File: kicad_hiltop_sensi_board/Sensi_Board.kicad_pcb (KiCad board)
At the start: 4 copper layers, 159.9 x 99.9 mm, 354 parts, among them J1 Conn_02x06_Counter_Clockwise, J10 Conn_ARM_JTAG_SWD_10, J2 Conn_02x06_Counter_Clockwise, J3 Conn_03x32_DIN41612, J4 Conn_02x06_Counter_Clockwise, J5 Conn_02x06_Counter_Clockwise, J6 Conn_02x06_Counter_Clockwise, J7 Conn_02x06_Counter_Clockwise, J8 Conn_02x06_Counter_Clockwise, K1 HRS1KH-S, Q10 ZXMN6A07F, Q11 ZXMN6A07F, Q2 ZXMN6A07F, Q7 ZXMN6A07F, Q8 ZXMN6A07F, SW1 SW_Push, SW2 SW_DIP_x04, SW3 SW_DIP_x04, SW4 SW_DIP_x04, SW5 SW_DIP_x04, U1 INA250A4, U10 MAX31865, U11 MAX31865, U13 CP2102N-A01-GQFN24, U14 BTS4140N, U15 BTS4140N, U16 MAX4194, U17 BTS4140N, U18 BTS4140N, U19 MAX4194, U2 LD1117S33TR_SOT223, U20 MAX4194, U21 MAX4194, U22 STM32F072RBTx, U23 MAX4194, U24 MAX4194, U25 MAX4194, U26 MAX4194, U27 USB2502, U3 AT25DN512CSSHF-B, U4 AD8646, U5 AD8646, U6 LM75B, U7 AT24C02C-SSHM-T, U8 MAX31865, U9 MAX31865, Y1 50ppm 24.000MHZ, Y2 8MHZ, Y3 ABS25-32.768KHZ-6-T

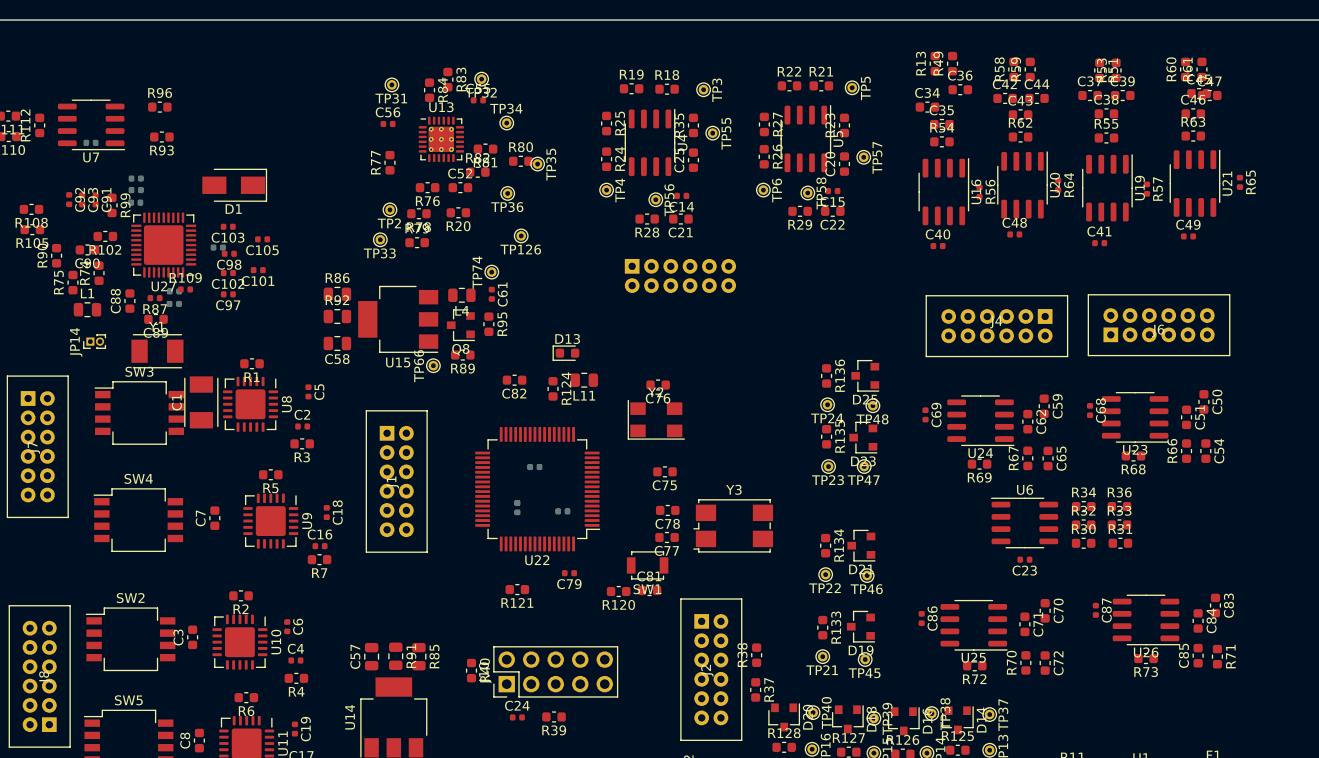
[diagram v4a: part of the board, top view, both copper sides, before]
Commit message: Updated sensi board pin map and layout before PCB tracking
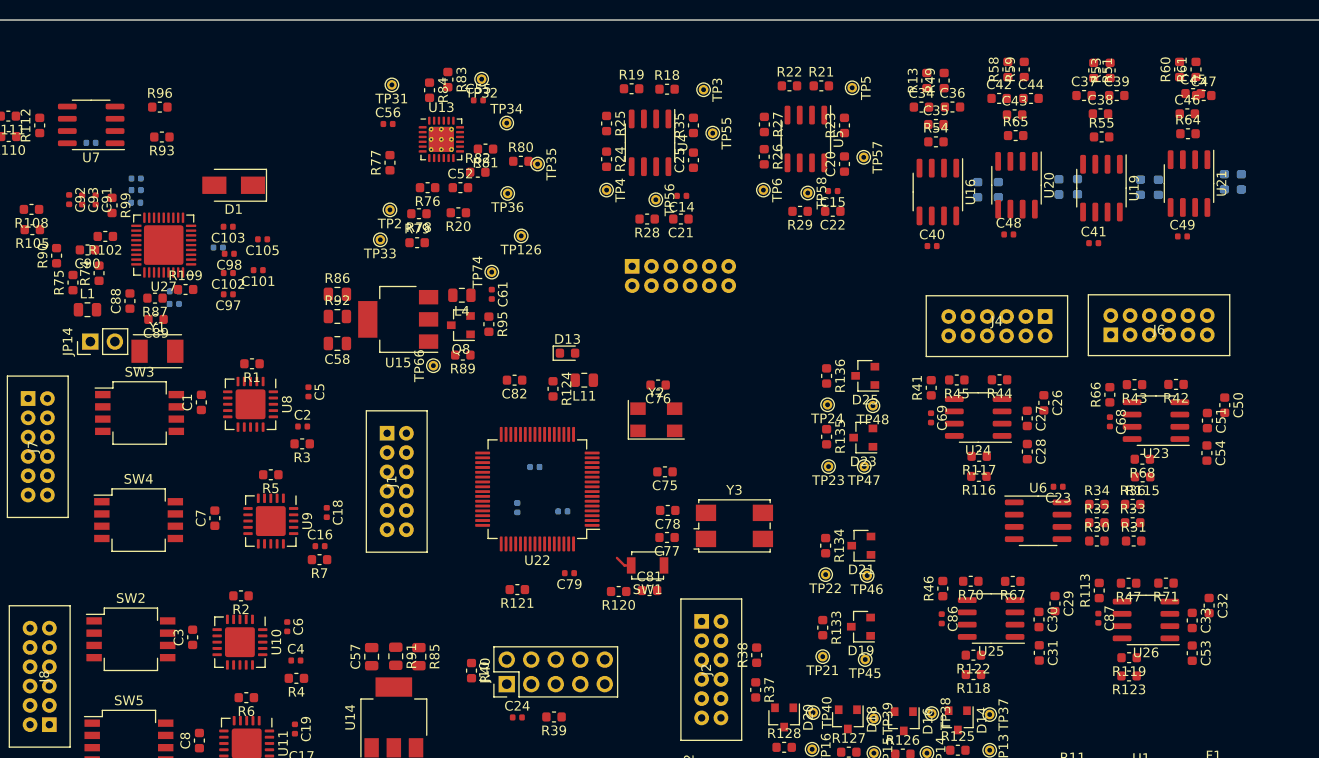
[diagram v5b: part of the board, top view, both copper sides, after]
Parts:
- removed C59, C65, C70, C72, C83, C85: Ccm, Capacitor_SMD:C_0603_1608Metric
- removed C62, C71, C84: Cdiff, Capacitor_SMD:C_0603_1608Metric
- added C26: Ccm, Capacitor_SMD:C_0603_1608Metric, F.Cu at (177.7, 84.8)
- added C27: Cdiff, Capacitor_SMD:C_0603_1608Metric, F.Cu at (175.9, 86.4)
- added C28: Ccm, Capacitor_SMD:C_0603_1608Metric, F.Cu at (175.9, 89.8)
- added C29: Ccm, Capacitor_SMD:C_0603_1608Metric, F.Cu at (178.8, 105.5)
- added C30: Cdiff, Capacitor_SMD:C_0603_1608Metric, F.Cu at (177.2, 107.2)
- added C31: Ccm, Capacitor_SMD:C_0603_1608Metric, F.Cu at (177.2, 110.7)
- added C32: Ccm, Capacitor_SMD:C_0603_1608Metric, F.Cu at (194.8, 105.8)
- added C33: Cdiff, Capacitor_SMD:C_0603_1608Metric, F.Cu at (193.0, 107.3)
- added C53: Ccm, Capacitor_SMD:C_0603_1608Metric, F.Cu at (193.0, 110.7)
- added R113: R, Resistor_SMD:R_0603_1608Metric, F.Cu at (183.4, 104.2)
- added R114: DNF, Resistor_SMD:R_0603_1608Metric, B.Cu at (181.2, 62.4)
- added R115: DNF, Resistor_SMD:R_0603_1608Metric, F.Cu at (187.9, 92.4)
- added R116: DNF, Resistor_SMD:R_0603_1608Metric, F.Cu at (170.9, 92.4)
- added R117: R, Resistor_SMD:R_0603_1608Metric, F.Cu at (171.0, 90.3)
- added R118: DNF, Resistor_SMD:R_0603_1608Metric, F.Cu at (170.4, 112.9)
- added R119: DNF, Resistor_SMD:R_0603_1608Metric, F.Cu at (186.5, 111.2)
- added R122: R, Resistor_SMD:R_0603_1608Metric, F.Cu at (170.4, 110.9)
- added R123: R, Resistor_SMD:R_0603_1608Metric, F.Cu at (186.5, 113.0)
- added R41: 0R, Resistor_SMD:R_0603_1608Metric, F.Cu at (166.0, 83.2)
- added R42: R, Resistor_SMD:R_0603_1608Metric, F.Cu at (191.4, 82.8)
- added R43: R, Resistor_SMD:R_0603_1608Metric, F.Cu at (187.1, 82.9)
- added R44: R, Resistor_SMD:R_0603_1608Metric, F.Cu at (173.1, 82.4)
- added R45: R, Resistor_SMD:R_0603_1608Metric, F.Cu at (168.6, 82.4)
- added R46: 0R, Resistor_SMD:R_0603_1608Metric, F.Cu at (167.2, 104.0)
- added R47: 0R, Resistor_SMD:R_0603_1608Metric, F.Cu at (186.4, 103.4)
- C1: footprint Crystal:Crystal_SMD_TXC_7A-2Pin_5x3.2mm -> Capacitor_SMD:C_0603_1608Metric
- C100, C102, C103, C104, C105: value 4.7uF 6.3V X5R -> 4.7uF
- C57, C58, C63, C64, R85, R86, R97, R98: value DNP -> DNF
- C91: value 1.0uF X5R 16V -> 1.0uF
- JP14: footprint Connector_PinHeader_1.00mm:PinHeader_1x02_P1.00mm_Vertical -> Connector_PinHeader_2.54mm:PinHeader_1x02_P2.54mm_Vertical
- L1: value FB 500mA/0.10DCR -> 500mA/0.10DCR
- R109, R87: footprint Resistor_SMD:R_0402_1005Metric -> Resistor_SMD:R_0603_1608Metric
- R56, R57: value 12K5 -> 12.4K; footprint Resistor_SMD:R_0402_1005Metric -> Resistor_SMD:R_0603_1608Metric; moved to B.Cu
- R62, R63: value 32R -> DNF; moved to B.Cu
- R64, R65: value 12K5 -> 32R; footprint Resistor_SMD:R_0402_1005Metric -> Resistor_SMD:R_0603_1608Metric
- R67, R70, R71: value 0R -> R
- R69: value 100R 0.1% -> 12.4K; moved to B.Cu
- R72: value R -> 12.4K; moved to B.Cu
- R73: value R -> DNF; moved to B.Cu
- moved R72 50.4 mm to (179.2, 62.4), turned to 270 degrees
- moved R73 50.4 mm to (198.1, 61.9), turned to 270 degrees
- moved R69 38.7 mm to (196.4, 61.8), turned to 270 degrees
- moved R65 23.7 mm to (174.7, 57.0), turned to 0 degrees
- moved R64 14.5 mm to (192.6, 56.9), turned to 0 degrees
- moved R67 12.8 mm to (174.4, 103.2), turned to 180 degrees
- moved R70 10.2 mm to (170.1, 103.2), turned to 180 degrees
- moved R66 9.86 mm to (184.5, 83.9)
- moved R71 9.30 mm to (190.3, 103.4), turned to 180 degrees
- moved C23 8.31 mm to (179.1, 93.4)
- moved R63 6.43 mm to (189.5, 62.4), turned to 270 degrees
- moved R62 5.93 mm to (172.9, 62.7), turned to 270 degrees
- moved C68 2.37 mm to (184.5, 86.7)
- moved C51 2.19 mm to (194.6, 86.6)
- moved U23 2.19 mm to (189.3, 86.6)
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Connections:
- net /STM_Micro/ADC13 renamed /STM_Micro/ADC8
- C20 pad 2: /ADC11 -> /ADC12
- C21 pad 2: /ADC10 -> /ADC13
- C22 pad 2: /ADC12 -> /ADC6
- C25 pad 2: /ADC9 -> /ADC7
- C50 pad 2: /TH1+ -> Net-(C50-Pad2)
- C51 pad 1: /TH1+ -> Net-(C50-Pad2)
- C51 pad 2: /TH1- -> Net-(C51-Pad2)
- C54 pad 1: /TH1- -> Net-(C51-Pad2)
- J5 pad 1: /ADC9 -> /ADC7
- J5 pad 12: /ADC12 -> /ADC6
- J5 pad 3: /ADC10 -> /ADC13
- J5 pad 5: /ADC11 -> /ADC12
- R23 pad 1: /ADC11 -> /ADC12
- R28 pad 1: /ADC10 -> /ADC13
- R29 pad 1: /ADC12 -> /ADC6
- R35 pad 1: /ADC9 -> /ADC7
- R62 pad 1: Net-(C42-Pad2) -> Net-(R56-Pad1)
- R62 pad 2: Net-(C43-Pad2) -> Net-(R56-Pad2)
- R63 pad 1: Net-(C45-Pad2) -> Net-(R57-Pad1)
- R63 pad 2: Net-(C46-Pad2) -> Net-(R57-Pad2)
- R64 pad 1: Net-(R64-Pad1) -> Net-(C45-Pad2)
- R64 pad 2: Net-(R64-Pad2) -> Net-(C46-Pad2)
- R65 pad 1: Net-(R65-Pad1) -> Net-(C42-Pad2)
- R65 pad 2: Net-(R65-Pad2) -> Net-(C43-Pad2)
- R67 pad 1: GND -> Net-(C29-Pad2)
- R67 pad 2: /TH3- -> /TH4+
- R70 pad 1: GND -> Net-(C30-Pad2)
- R71 pad 1: GND -> Net-(C32-Pad2)
- R71 pad 2: /TH2- -> /TH2+
- R72 pad 1: Net-(R72-Pad1) -> Net-(R114-Pad1)
- R72 pad 2: Net-(R72-Pad2) -> Net-(R114-Pad2)
- R73 pad 1: Net-(R73-Pad1) -> Net-(R69-Pad1)
- R73 pad 2: Net-(R73-Pad2) -> Net-(R69-Pad2)
- TP55 pad 1: /ADC9 -> /ADC7
- TP56 pad 1: /ADC10 -> /ADC13
- TP57 pad 1: /ADC11 -> /ADC12
- TP58 pad 1: /ADC12 -> /ADC6
- U16 pad 6: /ADC8 -> /ADC5
- U19 pad 6: /ADC6 -> /ADC3
- U20 pad 1: Net-(R64-Pad1) -> Net-(R114-Pad1)
- U20 pad 6: /ADC7 -> /ADC4
- U20 pad 8: Net-(R64-Pad2) -> Net-(R114-Pad2)
- U21 pad 1: Net-(R65-Pad1) -> Net-(R69-Pad1)
- U21 pad 6: /ADC5 -> /ADC2
- U21 pad 8: Net-(R65-Pad2) -> Net-(R69-Pad2)
- U22 pad 10: /ADC3 -> /ADC10
- U22 pad 11: /ADC2 -> /ADC11
- U22 pad 16: /ADC5 -> /ADC2
- U22 pad 17: /ADC6 -> /ADC3
- U22 pad 20: /ADC7 -> /ADC4
- U22 pad 22: /ADC8 -> /ADC5
- U22 pad 23: /ADC12 -> /ADC6
- U22 pad 24: /ADC11 -> /ADC12
- U22 pad 25: /ADC10 -> /ADC13
- U22 pad 26: /STM_RES2 -> /STM_RES1
- U22 pad 27: /ADC9 -> /ADC7
- U22 pad 28: /GPIO3 -> /STM_RES2
- U22 pad 40: /STM_RES1 -> /GPIO3
- U22 pad 51: Net-(R121-Pad2) -> (no net)
- U22 pad 53: (no net) -> Net-(R121-Pad2)
- U22 pad 9: /ADC4 -> /ADC9
- U23 pad 2: /TH1- -> Net-(C51-Pad2)
- U23 pad 3: /TH1+ -> Net-(C50-Pad2)
- U23 pad 6: /ADC2 -> /ADC11
- U24 pad 1: Net-(R69-Pad1) -> Net-(R116-Pad1)
- U24 pad 2: /TH3- -> Net-(C27-Pad2)
- U24 pad 3: /TH3+ -> Net-(C26-Pad2)
- U24 pad 8: Net-(R69-Pad2) -> Net-(R116-Pad2)
- U25 pad 1: Net-(R72-Pad1) -> Net-(R118-Pad1)
- U25 pad 2: /TH4- -> Net-(C30-Pad2)
- U25 pad 3: /TH4+ -> Net-(C29-Pad2)
- U25 pad 6: /ADC4 -> /ADC9
- U25 pad 8: Net-(R72-Pad2) -> Net-(R118-Pad2)
- U26 pad 1: Net-(R73-Pad1) -> Net-(R119-Pad1)
- U26 pad 2: /TH2- -> Net-(C33-Pad2)
- U26 pad 3: /TH2+ -> Net-(C32-Pad2)
- U26 pad 6: /ADC3 -> /ADC10
- U26 pad 8: Net-(R73-Pad2) -> Net-(R119-Pad2)
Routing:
- net /STM_RESET: track 0.00 -> 1.80 mm

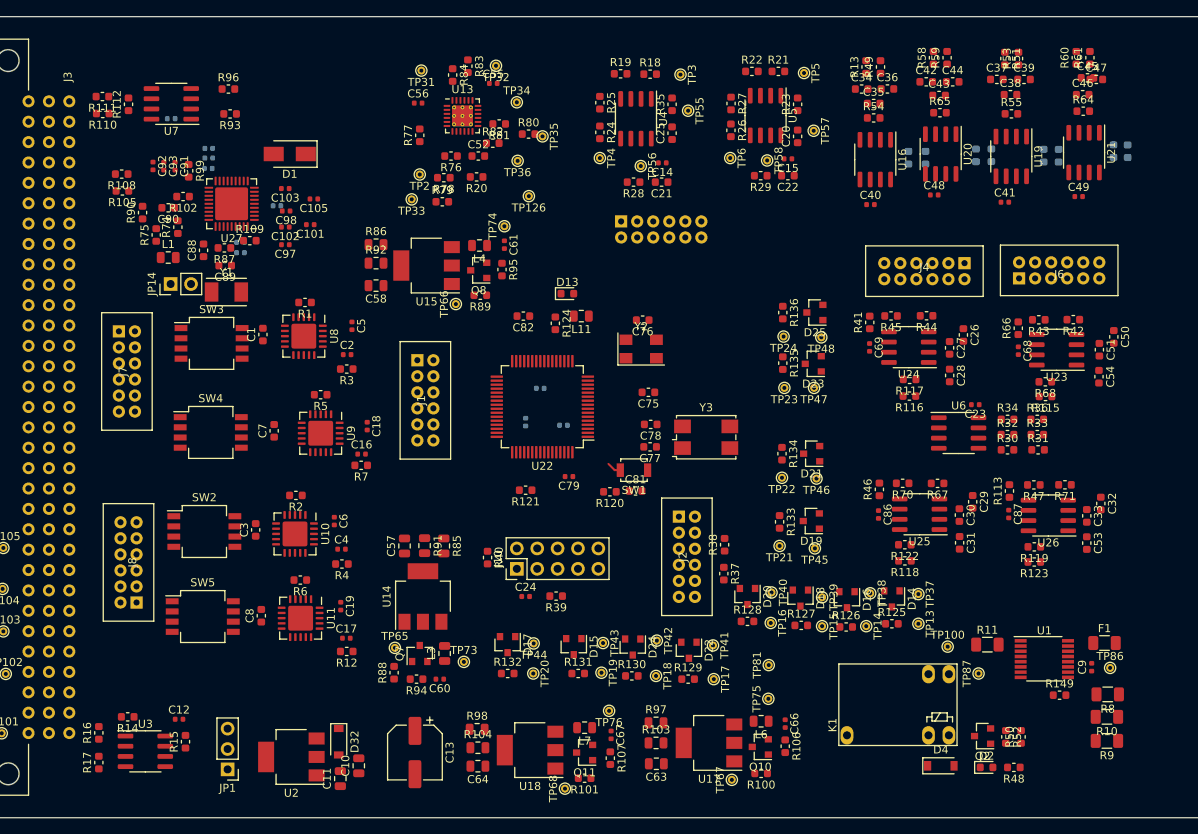
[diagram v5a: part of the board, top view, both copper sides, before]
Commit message: Started PCB routing of Sensi Board LBBC
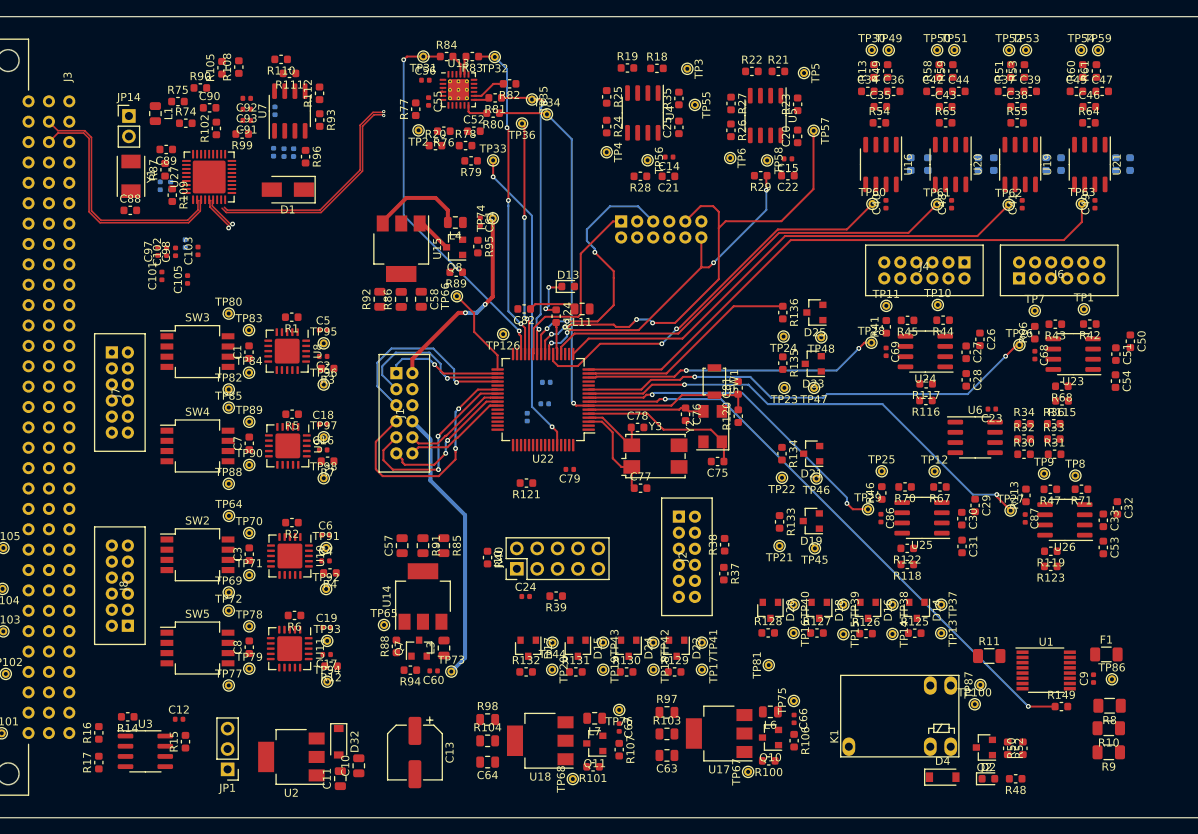
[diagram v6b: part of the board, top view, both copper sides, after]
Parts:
- added TP1: Test_Point, TestPoint:TestPoint_THTPad_D1.0mm_Drill0.5mm, F.Cu at (192.7, 81.5)
- added TP10: Test_Point, TestPoint:TestPoint_THTPad_D1.0mm_Drill0.5mm, F.Cu at (174.5, 81.0)
- added TP11: Test_Point, TestPoint:TestPoint_THTPad_D1.0mm_Drill0.5mm, F.Cu at (168.1, 81.1)
- added TP12: Test_Point, TestPoint:TestPoint_THTPad_D1.0mm_Drill0.5mm, F.Cu at (174.1, 101.8)
- added TP25: Test_Point, TestPoint:TestPoint_THTPad_D1.0mm_Drill0.5mm, F.Cu at (167.5, 101.7)
- added TP26: Test_Point, TestPoint:TestPoint_THTPad_D1.0mm_Drill0.5mm, F.Cu at (184.6, 86.0)
- added TP27: Test_Point, TestPoint:TestPoint_THTPad_D1.0mm_Drill0.5mm, F.Cu at (183.6, 106.6)
- added TP28: Test_Point, TestPoint:TestPoint_THTPad_D1.0mm_Drill0.5mm, F.Cu at (166.2, 85.7)
- added TP29: Test_Point, TestPoint:TestPoint_THTPad_D1.0mm_Drill0.5mm, F.Cu at (165.8, 106.5)
- added TP30: Test_Point, TestPoint:TestPoint_THTPad_D1.0mm_Drill0.5mm, F.Cu at (166.2, 49.2)
- added TP49: Test_Point, TestPoint:TestPoint_THTPad_D1.0mm_Drill0.5mm, F.Cu at (168.4, 49.2)
- added TP50: Test_Point, TestPoint:TestPoint_THTPad_D1.0mm_Drill0.5mm, F.Cu at (174.4, 49.2)
- added TP51: Test_Point, TestPoint:TestPoint_THTPad_D1.0mm_Drill0.5mm, F.Cu at (176.5, 49.2)
- added TP52: Test_Point, TestPoint:TestPoint_THTPad_D1.0mm_Drill0.5mm, F.Cu at (183.4, 49.2)
- added TP53: Test_Point, TestPoint:TestPoint_THTPad_D1.0mm_Drill0.5mm, F.Cu at (185.5, 49.2)
- added TP54: Test_Point, TestPoint:TestPoint_THTPad_D1.0mm_Drill0.5mm, F.Cu at (192.3, 49.2)
- added TP59: Test_Point, TestPoint:TestPoint_THTPad_D1.0mm_Drill0.5mm, F.Cu at (194.5, 49.2)
- added TP60: Test_Point, TestPoint:TestPoint_THTPad_D1.0mm_Drill0.5mm, F.Cu at (166.3, 68.4)
- added TP61: Test_Point, TestPoint:TestPoint_THTPad_D1.0mm_Drill0.5mm, F.Cu at (174.4, 68.5)
- added TP62: Test_Point, TestPoint:TestPoint_THTPad_D1.0mm_Drill0.5mm, F.Cu at (183.3, 68.5)
- added TP63: Test_Point, TestPoint:TestPoint_THTPad_D1.0mm_Drill0.5mm, F.Cu at (192.4, 68.4)
- added TP64: Test_Point, TestPoint:TestPoint_THTPad_D1.0mm_Drill0.5mm, F.Cu at (86.1, 107.3)
- added TP69: Test_Point, TestPoint:TestPoint_THTPad_D1.0mm_Drill0.5mm, F.Cu at (86.1, 116.8)
- added TP7: Test_Point, TestPoint:TestPoint_THTPad_D1.0mm_Drill0.5mm, F.Cu at (186.6, 81.7)
- added TP70: Test_Point, TestPoint:TestPoint_THTPad_D1.0mm_Drill0.5mm, F.Cu at (88.7, 109.4)
- added TP71: Test_Point, TestPoint:TestPoint_THTPad_D1.0mm_Drill0.5mm, F.Cu at (88.7, 114.7)
- added TP72: Test_Point, TestPoint:TestPoint_THTPad_D1.0mm_Drill0.5mm, F.Cu at (86.1, 119.1)
- added TP77: Test_Point, TestPoint:TestPoint_THTPad_D1.0mm_Drill0.5mm, F.Cu at (86.1, 128.4)
- added TP78: Test_Point, TestPoint:TestPoint_THTPad_D1.0mm_Drill0.5mm, F.Cu at (88.7, 121.1)
- added TP79: Test_Point, TestPoint:TestPoint_THTPad_D1.0mm_Drill0.5mm, F.Cu at (88.7, 126.3)
- added TP8: Test_Point, TestPoint:TestPoint_THTPad_D1.0mm_Drill0.5mm, F.Cu at (191.6, 102.3)
- added TP80: Test_Point, TestPoint:TestPoint_THTPad_D1.0mm_Drill0.5mm, F.Cu at (86.1, 82.1)
- added TP82: Test_Point, TestPoint:TestPoint_THTPad_D1.0mm_Drill0.5mm, F.Cu at (86.1, 91.5)
- added TP83: Test_Point, TestPoint:TestPoint_THTPad_D1.0mm_Drill0.5mm, F.Cu at (88.6, 84.1)
- added TP84: Test_Point, TestPoint:TestPoint_THTPad_D1.0mm_Drill0.5mm, F.Cu at (88.6, 89.5)
- added TP85: Test_Point, TestPoint:TestPoint_THTPad_D1.0mm_Drill0.5mm, F.Cu at (86.1, 93.8)
- added TP88: Test_Point, TestPoint:TestPoint_THTPad_D1.0mm_Drill0.5mm, F.Cu at (86.1, 103.3)
- added TP89: Test_Point, TestPoint:TestPoint_THTPad_D1.0mm_Drill0.5mm, F.Cu at (88.7, 95.6)
- added TP9: Test_Point, TestPoint:TestPoint_THTPad_D1.0mm_Drill0.5mm, F.Cu at (187.7, 102.0)
- added TP90: Test_Point, TestPoint:TestPoint_THTPad_D1.0mm_Drill0.5mm, F.Cu at (88.7, 101.0)
- added TP91: Test_Point, TestPoint:TestPoint_THTPad_D1.0mm_Drill0.5mm, F.Cu at (98.2, 111.3)
- added TP92: Test_Point, TestPoint:TestPoint_THTPad_D1.0mm_Drill0.5mm, F.Cu at (98.2, 116.4)
- added TP93: Test_Point, TestPoint:TestPoint_THTPad_D1.0mm_Drill0.5mm, F.Cu at (98.4, 122.9)
- added TP94: Test_Point, TestPoint:TestPoint_THTPad_D1.0mm_Drill0.5mm, F.Cu at (98.4, 128.0)
- added TP95: Test_Point, TestPoint:TestPoint_THTPad_D1.0mm_Drill0.5mm, F.Cu at (97.9, 85.8)
- added TP96: Test_Point, TestPoint:TestPoint_THTPad_D1.0mm_Drill0.5mm, F.Cu at (97.9, 90.9)
- added TP97: Test_Point, TestPoint:TestPoint_THTPad_D1.0mm_Drill0.5mm, F.Cu at (97.9, 97.5)
- added TP98: Test_Point, TestPoint:TestPoint_THTPad_D1.0mm_Drill0.5mm, F.Cu at (97.9, 102.6)
- R54, R55, R64, R65: value 32R -> 30R
- moved R112 23.8 mm to (97.4, 54.6)
- moved R111 23.5 mm to (93.7, 52.1)
- moved R110 23.2 mm to (92.6, 50.4)
- moved JP14 21.6 mm to (73.7, 57.5), turned to 0 degrees
- moved R108 19.8 mm to (87.3, 51.4), turned to 90 degrees
- moved R105 19.7 mm to (85.2, 51.4), turned to 90 degrees
- moved C101 19.6 mm to (77.8, 77.4), turned to 90 degrees
- moved Y1 18.7 mm to (73.9, 65.0), turned to 270 degrees
- moved C105 18.7 mm to (81.0, 77.8), turned to 90 degrees
- moved R120 18.6 mm to (149.6, 94.9), turned to 90 degrees
- moved C81 18.1 mm to (149.6, 91.3), turned to 90 degrees
- moved L1 18.0 mm to (77.0, 57.2), turned to 270 degrees
- moved TP126 17.5 mm to (120.3, 84.7)
- moved R90 17.1 mm to (82.5, 54.0), turned to 0 degrees
- moved R75 16.8 mm to (79.8, 55.7), turned to 0 degrees
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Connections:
- U27 pad 5: /USB_DEBUG_N -> /STM_USB_DATA_N
- U27 pad 6: /USB_DEBUG_P -> /STM_USB_DATA_P
- U27 pad 8: /STM_USB_DATA_P -> /USB_DEBUG_P
- U27 pad 9: /STM_USB_DATA_N -> /USB_DEBUG_N
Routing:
- net /STM_Micro/ADC8: track 0.00 -> 74.1 mm, vias 0 -> 2
- net /ADC2: track 0.00 -> 71.4 mm
- net /STM_RESET: track 1.80 -> 66.5 mm, vias 0 -> 1
- net /ADC3: track 0.00 -> 62.0 mm
- net /ADC12: track 0.00 -> 61.8 mm, vias 0 -> 4
- net /ADC10: track 0.00 -> 59.7 mm, vias 0 -> 2
- net /ADC11: track 0.00 -> 58.1 mm, vias 0 -> 2
- net /ADC4: track 0.00 -> 55.1 mm
- net /ADC5: track 0.00 -> 49.3 mm, vias 0 -> 2
- net /STM_DEBUG_RX: track 0.00 -> 47.5 mm, vias 0 -> 2
- net /ADC6: track 0.00 -> 43.5 mm, vias 0 -> 4
- net /ADC9: track 0.00 -> 41.5 mm, vias 0 -> 2
- net /STM_DEBUG_TX: track 0.00 -> 40.6 mm, vias 0 -> 3
- net /STM_BOOT0: track 0.00 -> 38.8 mm, vias 0 -> 2
- net /STM_RES1: track 0.00 -> 37.7 mm, vias 0 -> 2
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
